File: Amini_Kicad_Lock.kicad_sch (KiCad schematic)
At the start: 40 parts, among them J1 Conn_01x02_Pin, J2 Conn_01x04, J3 MM8130-2600RA2, J4 Conn_01x03_Pin, U1 nRF5340-QKxx, X1 ${ALTIUM_VALUE}, X2 ${ALTIUM_VALUE}

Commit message: Wireing done, no error
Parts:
- L2: footprint INDC1608X06L -> Nordic_Semiconductor:INDC1608X06L
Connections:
- net LED2: now reaches U1.AL27 (P0.24)
- net LED2: now also J4.2 (Pin_2), LED2.1 (C)
- net LED1: now reaches U1.AL29 (AIN5/P0.26)
- net LED1: now also J4.1 (Pin_1), LED1.1 (C)
- net LED3: now reaches U1.AL9 (IO3/P0.16)
- net LED3: now also J4.3 (Pin_3), LED3.1 (C)
- removed net P0.28/AIN7: J4.1 (Pin_1), LED1.1 (C), U1.AE31 (AIN7/P0.28)
- removed net P0.29: J4.2 (Pin_2), LED2.1 (C), U1.U31 (P0.29)
- removed net P0.30: J4.3 (Pin_3), LED3.1 (C), U1.B24 (P0.30)
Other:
- note added: "Kan hende jeg har køddet til foodprint, dobbeltsjekk"
- moved on the sheet: A1
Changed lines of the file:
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@@
 	(wire
 		(pts
-			(xy 144.78 100.33) (xy 181.61 100.33)
+			(xy 144.78 64.77) (xy 181.61 64.77)
 		)
 		(stroke
@@
 	(wire
 		(pts
-			(xy 48.26 115.57) (xy 40.64 115.57)
+			(xy 45.72 115.57) (xy 40.64 115.57)
 		)
 		(stroke
@@
 	(wire
 		(pts
+			(xy 144.78 90.17) (xy 194.31 90.17)
+		)
+		(stroke
+			(width 0)
+			(type default)
+		)
+	)
+	(wire
+		(pts
 			(xy 269.24 109.22) (xy 266.7 109.22)
 		)
@@
 	(wire
 		(pts
-			(xy 144.78 97.79) (xy 187.96 97.79)
-		)
-		(stroke
-			(width 0)
-			(type default)
-		)
-	)
-	(wire
-		(pts
 			(xy 234.95 121.92) (xy 234.95 129.54)
 		)
@@
 	(wire
 		(pts
-			(xy 144.78 95.25) (xy 194.31 95.25)
+			(xy 213.36 118.11) (xy 199.39 118.11)
 		)
 		(stroke
@@
 	(wire
 		(pts
-			(xy 213.36 118.11) (xy 199.39 118.11)
+			(xy 60.96 153.67) (xy 60.96 156.21)
 		)
 		(stroke
@@
 	(wire
 		(pts
-			(xy 60.96 153.67) (xy 60.96 156.21)
+			(xy 189.23 120.65) (xy 199.39 120.65)
 		)
 		(stroke
@@
 	(wire
 		(pts
-			(xy 189.23 120.65) (xy 199.39 120.65)
+			(xy 144.78 24.13) (xy 144.78 19.05)
 		)
 		(stroke
@@
 	(wire
 		(pts
-			(xy 144.78 24.13) (xy 144.78 19.05)
+			(xy 234.95 129.54) (xy 259.08 129.54)
 		)
 		(stroke
@@
 	(wire
 		(pts
-			(xy 234.95 129.54) (xy 259.08 129.54)
+			(xy 144.78 85.09) (xy 187.96 85.09)
 		)
 		(stroke
@@
 	(wire
 		(pts
-			(xy 48.26 114.3) (xy 48.26 115.57)
+			(xy 45.72 114.3) (xy 45.72 115.57)
 		)
 		(stroke
@@
 		)
 	)
-	(label "P0.29"
+	(text "Kan hende jeg har køddet til foodprint, dobbeltsjekk\n"
+		(exclude_from_sim no)
+		(at 54.102 80.264 0)
+		(effects
+			(font
+				(size 1.27 1.27)
+			)
+		)
+	)
+	(label "LED2"
 		(at 241.3 119.38 0)
 		(fields_autoplaced yes)
@@
 		)
 	)
-	(label "P0.28/AIN7"
+	(label "LED1"
 		(at 241.3 109.22 0)
 		(fields_autoplaced yes)
@@
 		)
 	)
-	(label "P0.29"
-		(at 171.45 97.79 0)
+	(label "SWDCLK"
+		(at 212.09 62.23 0)
 		(fields_autoplaced yes)
 		(effects
@@
 		)
 	)
-	(label "SWDCLK"
-		(at 212.09 62.23 0)
+	(label "LED2"
+		(at 168.91 85.09 0)
 		(fields_autoplaced yes)
 		(effects
@@
 		)
 	)
-	(label "P0.28/AIN7"
-		(at 171.45 95.25 0)
+	(label "LED3"
+		(at 172.72 64.77 0)
 		(fields_autoplaced yes)
 		(effects
@@
 		)
 	)
-	(label "P0.30"
-		(at 171.45 100.33 0)
+	(label "LED1"
+		(at 166.37 90.17 0)
 		(fields_autoplaced yes)
 		(effects
@@
 		)
 	)
-	(label "P0.30"
+	(label "LED3"
 		(at 241.3 129.54 0)
 		(fields_autoplaced yes)
@@
 	(symbol
 		(lib_id "pca10143_sheet2_nrf5340_mcu-altium-import:root_0_Antenna with GND")
-		(at 48.26 110.49 0)
+		(at 45.72 110.49 0)
 		(unit 1)
 		(exclude_from_sim no)
@@
 		(dnp no)
 		(property "Reference" "A1"
-			(at 44.196 105.156 0)
+			(at 41.656 105.156 0)
 			(effects
 				(font
@@
 		)
 		(property "Value" "${ALTIUM_VALUE}"
-			(at 52.07 113.03 0)
+			(at 49.53 113.03 0)
 			(effects
 				(font
@@
 		)
 		(property "Footprint" "Nordic_Semiconductor:2450AT18D0100_STD-R"
-			(at 48.26 110.49 0)
+			(at 45.72 110.49 0)
 			(effects
 				(font
@@
 		)
 		(property "Datasheet" ""
-			(at 48.26 110.49 0)
+			(at 45.72 110.49 0)
 			(effects
 				(font
@@
 		)
 		(property "Description" "2.45 GHz chip antenna"
-			(at 48.26 110.49 0)
+			(at 45.72 110.49 0)
 			(effects
 				(font
@@
 		)
 		(property "PART NUMBER" "Johanson 2450AT18D0100_STD-R"
-			(at 44.196 105.156 0)
+			(at 41.656 105.156 0)
 			(effects
 				(font
@@
 		)
 		(property "PARTID" "100700005"
-			(at 44.196 105.156 0)
+			(at 41.656 105.156 0)
 			(effects
 				(font
@@
 		)
 		(property "COMPONENT CLASS" "Antennas"
-			(at 44.196 105.156 0)
+			(at 41.656 105.156 0)
 			(effects
 				(font
@@
 		)
 		(property "AUTHOR" "rsk"
-			(at 44.196 105.156 0)
+			(at 41.656 105.156 0)
 			(effects
 				(font
@@
 		)
 		(property "MANUFACTURER" "Johanson Technology"
-			(at 44.196 105.156 0)
+			(at 41.656 105.156 0)
 			(effects
 				(font
@@
 		)
 		(property "MANUFACTURER PART NUMBER" "2450AT18D0100"
-			(at 44.196 105.156 0)
+			(at 41.656 105.156 0)
 			(effects
 				(font
@@
 		)
 		(property "COMPONENTLINK1URL" "N.A."
-			(at 44.196 105.156 0)
+			(at 41.656 105.156 0)
 			(effects
 				(font
@@
 		)
 		(property "COMPONENTLINK1DESCRIPTION" "Datasheet"
-			(at 44.196 105.156 0)
+			(at 41.656 105.156 0)
 			(effects
 				(font
@@
 		)
 		(property "COMPONENTLINK2URL" "N.A."
-			(at 44.196 105.156 0)
+			(at 41.656 105.156 0)
 			(effects
 				(font
@@
 		)
 		(property "COMPONENTLINK2DESCRIPTION" "Supplier link"
-			(at 44.196 105.156 0)
+			(at 41.656 105.156 0)
 			(effects
 				(font
@@
 		)
 		(property "HELPURL" "http://www.johansontechnology.com/datasheets/antennas/2450AT18D0100.pdf"
-			(at 44.196 105.156 0)
+			(at 41.656 105.156 0)
 			(effects
 				(font
@@
 		)
 		(property "FOOTPRINT DOC" "2450AT18D0100"
-			(at 44.196 105.156 0)
+			(at 41.656 105.156 0)
 			(effects
 				(font
@@
 		)
 		(property "LATESTREVISIONDATE" "2016-06-02"
-			(at 44.196 105.156 0)
+			(at 41.656 105.156 0)
 			(effects
 				(font
@@
 		)
 		(property "PAD COUNT" "4"
-			(at 44.196 105.156 0)
+			(at 41.656 105.156 0)
 			(effects
 				(font
@@
 		)
 		(property "PUBLISHED" "2016-01-12"
-			(at 44.196 105.156 0)
+			(at 41.656 105.156 0)
 			(effects
 				(font
@@
 		)
 		(property "ALTIUM_VALUE" "2450AT18D0100"
-			(at 44.196 105.156 0)
+			(at 41.656 105.156 0)
 			(effects
 				(font
@@
 		)
 		(property "NOTE" "N.A."
-			(at 44.196 105.156 0)
+			(at 41.656 105.156 0)
 			(effects
 				(font
@@
 		)
 		(property "SUPPLIER 1" "Digi-Key"
-			(at 44.196 105.156 0)
+			(at 41.656 105.156 0)
 			(effects
 				(font
@@
 		)
 		(property "SUPPLIER PART NUMBER 1" "2450AT18D0100E"
-			(at 44.196 105.156 0)
+			(at 41.656 105.156 0)
 			(effects
 				(font
@@
 		)
 		(property "SUPPLIER 2" "Mouser"
-			(at 44.196 105.156 0)
+			(at 41.656 105.156 0)
 			(effects
 				(font
@@
 		)
 		(property "SUPPLIER PART NUMBER 2" "609-2450AT18D0100E"
-			(at 44.196 105.156 0)
+			(at 41.656 105.156 0)
 			(effects
 				(font
@@
 		)
 		(property "ARTIKKELNR NOCA" "53059035"
-			(at 44.196 105.156 0)
+			(at 41.656 105.156 0)
 			(effects
 				(font
@@
 		)
 		(property "PART NUMBER IPS" "00000001415"
-			(at 44.196 105.156 0)
+			(at 41.656 105.156 0)
 			(effects
 				(font
@@
 		)
 		(property "PART NUMBER NORAUTRON" "N.A."
-			(at 44.196 105.156 0)
+			(at 41.656 105.156 0)
 			(effects
 				(font
@@
 		)
 		(property "ASSEMBLY" ""
-			(at 44.196 105.156 0)
+			(at 41.656 105.156 0)
 			(effects
 				(font
@@
 		)
 		(property "COMPONENT STATUS" "Active"
-			(at 44.196 102.616 0)
+			(at 41.656 102.616 0)
 			(effects
 				(font
@@
 		)
 		(property "PART NUMBER NEMS" "100700005"
-			(at 44.196 102.616 0)
+			(at 41.656 102.616 0)
 			(effects
 				(font
@@
 			)
 		)
-		(property "Footprint" "INDC1608X06L"
+		(property "Footprint" "Nordic_Semiconductor:INDC1608X06L"
 			(at 50.8 85.09 0)
 			(effects

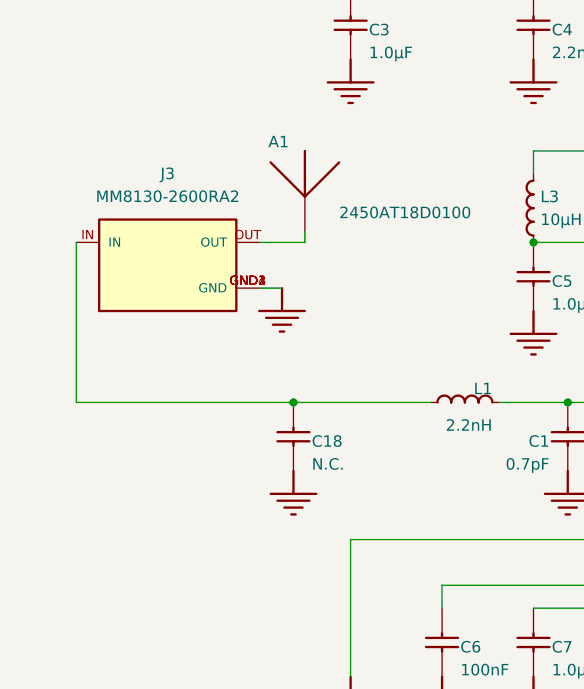
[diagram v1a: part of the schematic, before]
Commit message: Backup of wrong way, went with two matching netwrk, konstanting gave me a heds up that i need only one and take ohm in wire into consideration
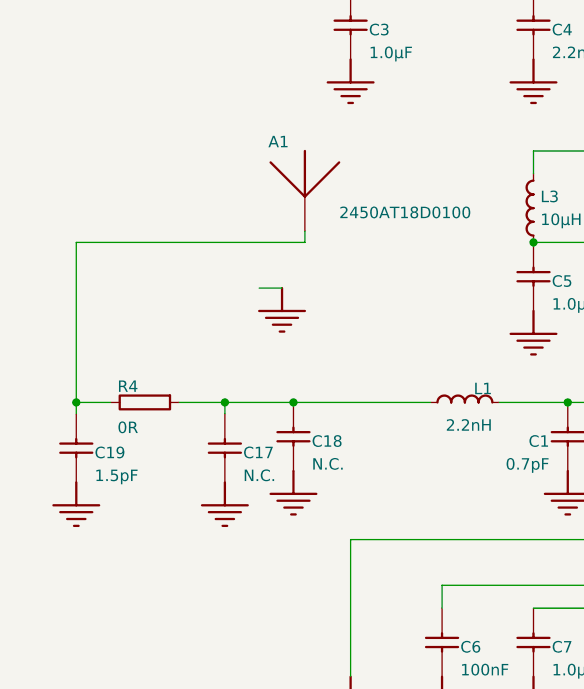
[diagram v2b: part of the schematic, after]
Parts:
- removed J3: MM8130-2600RA2, MM8130-2600RA2 antenna:MURATA_MM8130-2600RA2, symbol MM8130-2600RA2:MM8130-2600RA2
- added C17: ${ALTIUM_VALUE}, Inductor_SMD:L_0603_1608Metric, symbol 400250-altium-import:root_3_CAP
- added C19: ${ALTIUM_VALUE}, Inductor_SMD:L_0603_1608Metric, symbol 400250-altium-import:root_1_CAP
- added R4: ${ALTIUM_VALUE}, Resistor_SMD:R_0603_1608Metric, symbol 400250-altium-import:root_0_RES
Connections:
- net GND: now also C17.2, C19.1
- net at C18.2, L1.2: now also C17.1, R4.2
- net at A1.1: now also C19.2, R4.1
